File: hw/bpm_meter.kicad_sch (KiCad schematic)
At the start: 57 parts, among them J1 weidmueller_SL5.08HC-06-90, J2 weidmueller_SL5.08HC-10-90, Q1 AO3400A, SW1 dip_switch_SPST16, U1 SP3485EN-L/TR, U2 AOZ1282CI

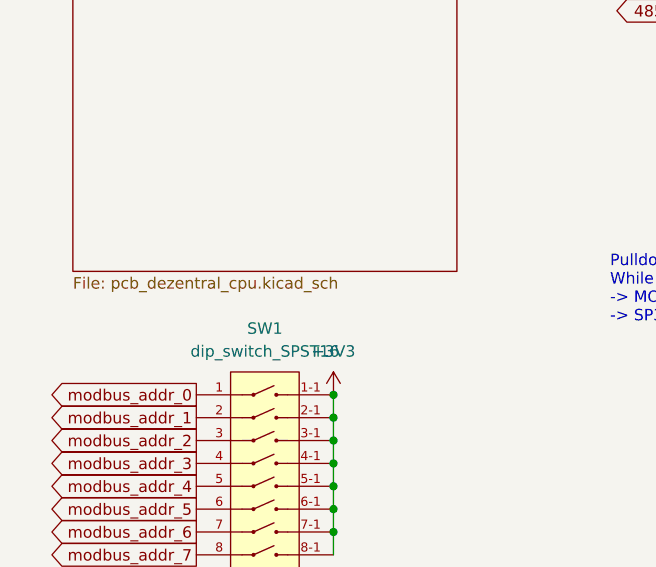
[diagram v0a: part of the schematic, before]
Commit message: Renamed the KiCad project
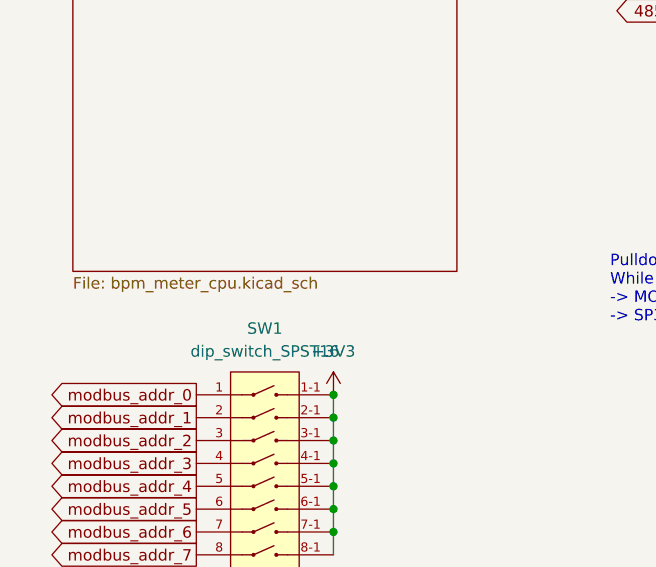
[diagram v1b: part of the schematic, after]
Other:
- sheet cpu: file pcb_dezentral_cpu.kicad_sch -> bpm_meter_cpu.kicad_sch
- company: www.positron.ch -> (none)
- title: Heizung Pünterswis - pcb_dezentral -> Schen-Key BPM Meter

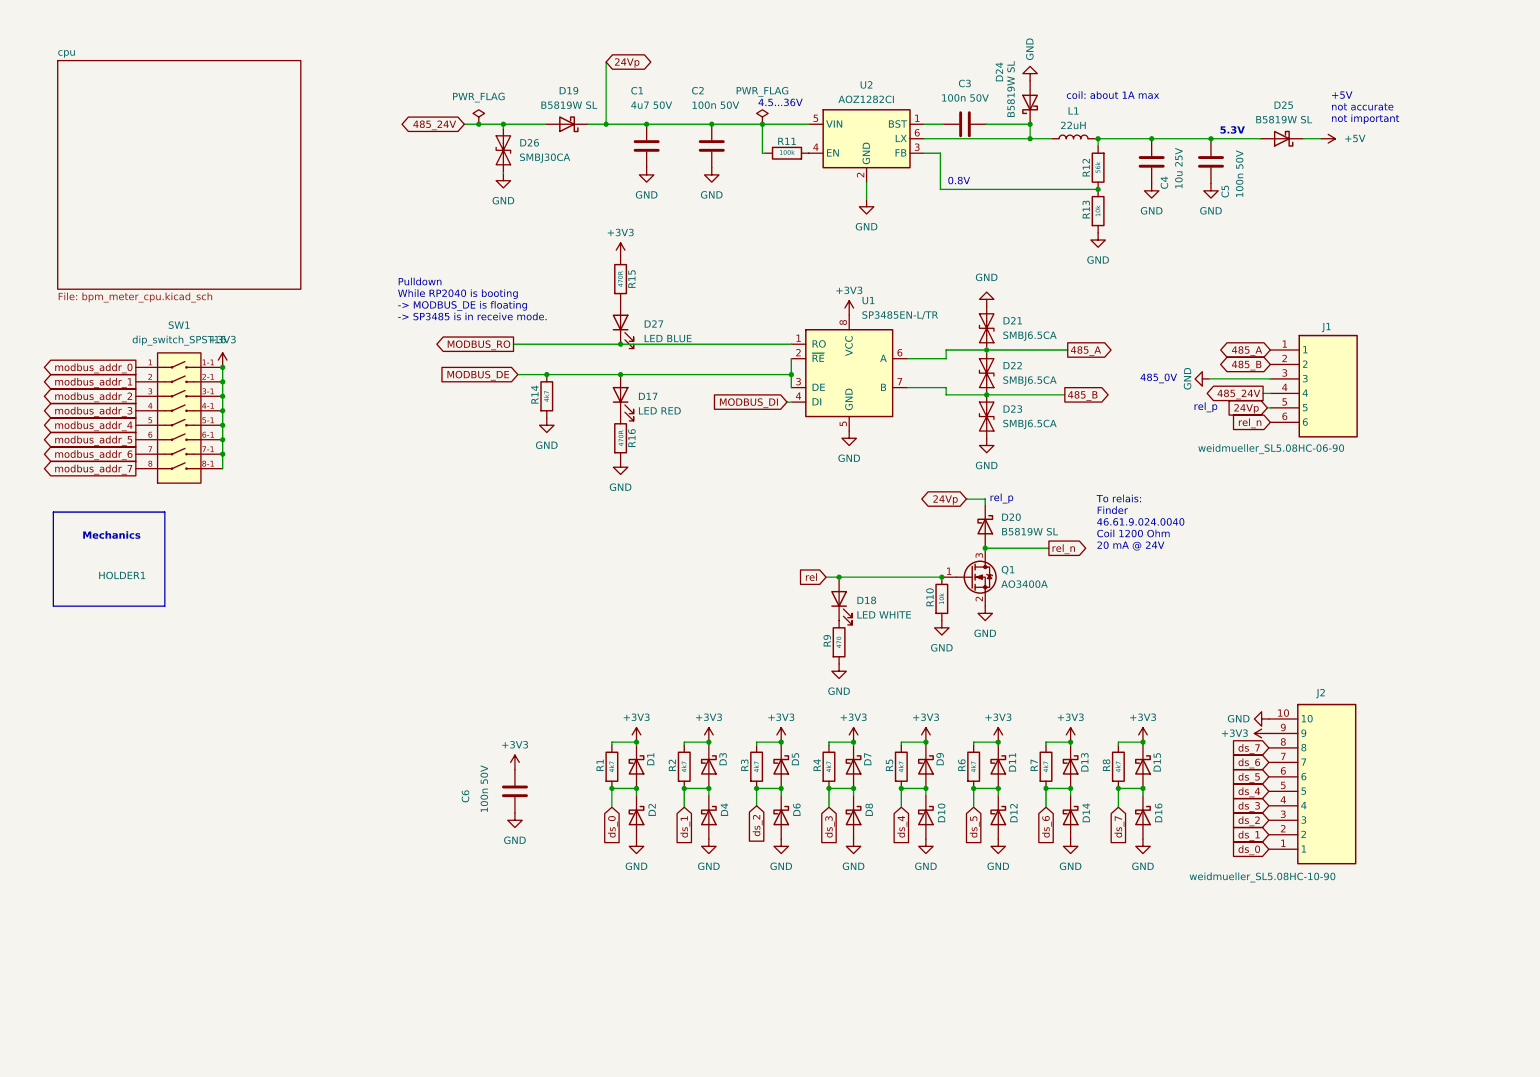
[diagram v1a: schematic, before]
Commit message: Removed unused stuff and added beat input
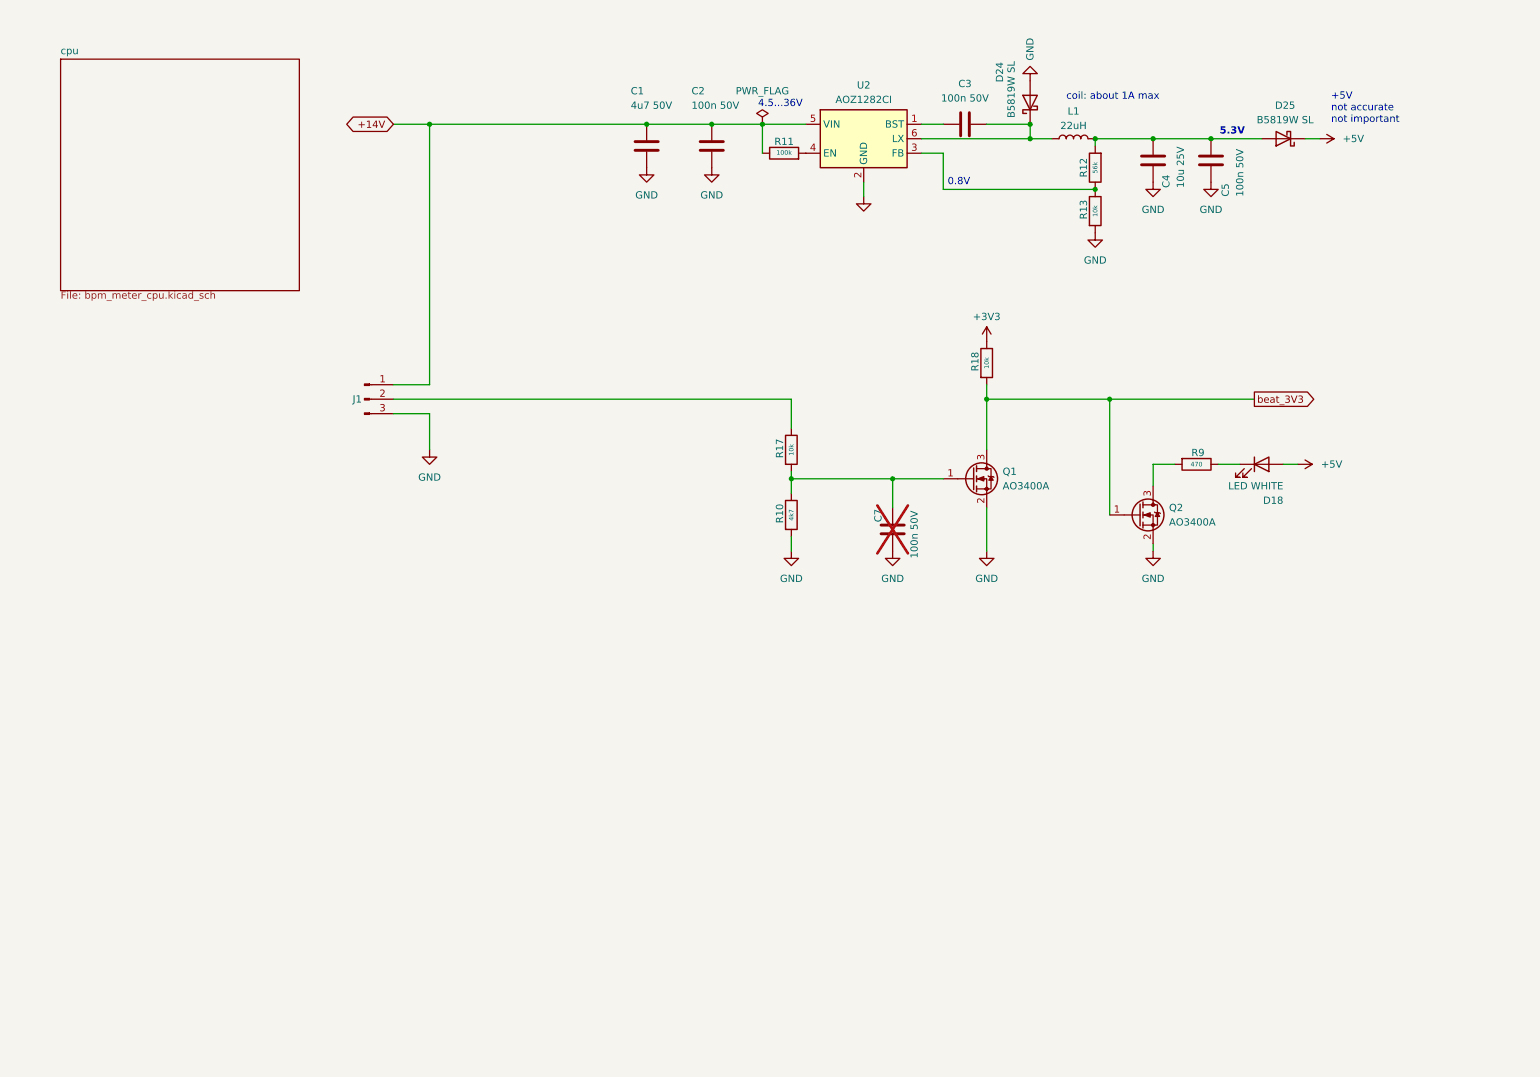
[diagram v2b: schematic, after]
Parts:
- removed C6: 100n 50V, Diode_SMD:D_0805_2012Metric, symbol Device:C
- removed D1, D10, D11, D12, D13, D14, D15, D16, D19, D2, D20, D3, D4, D5, D6, D7, D8, D9: B5819W SL, Diode_SMD:D_SOD-123, symbol Device:D_Schottky
- removed D17: LED RED, 00_project_library:LED_0603_1608Metric, symbol 00_project_library:LED RED
- removed D21, D22, D23: SMBJ6.5CA, Diode_SMD:D_SMB, symbol Diode:SMAJ64CA
- removed D26: SMBJ30CA, Diode_SMD:D_SMB, symbol Diode:SMAJ64CA
- removed D27: LED BLUE, 00_project_library:LED_0603_1608Metric, symbol 00_project_library:LED BLUE
- removed J1: weidmueller_SL5.08HC-06-90, 00_project_library:weidmueller_SL5.08HC-06-90, symbol 00_project_library:weidmueller_SL5.08HC-06-90
- removed J2: weidmueller_SL5.08HC-10-90, 00_project_library:weidmueller_SL5.08HC-10-90, symbol 00_project_library:weidmueller_SL5.08HC-10-90
- removed R1, R14, R2, R3, R4, R5, R6, R7, R8: 4k7, Resistor_SMD:R_0402_1005Metric_Pad0.72x0.64mm_HandSolder, symbol Device:R
- removed R15, R16: 470R, Resistor_SMD:R_0402_1005Metric_Pad0.72x0.64mm_HandSolder, symbol Device:R
- removed SW1: dip_switch_SPST16, 00_project_library:dip_switch_SPST16, symbol 00_project_library:dip_switch_SPST16
- removed U1: SP3485EN-L/TR, Package_SO:SOIC-8_3.9x4.9mm_P1.27mm, symbol 00_project_library:modbus_SP3485EN
- added C7: 100n 50V, Diode_SMD:D_0805_2012Metric, symbol Device:C
- added J1: Conn_01x03_Pin, Connector_PinHeader_2.54mm:PinHeader_1x03_P2.54mm_Vertical, symbol Connector:Conn_01x03_Pin
- added Q2: AO3400A, Package_TO_SOT_SMD:SOT-23, symbol Transistor_FET:AO3400A
- added R17, R18: 10k, Resistor_SMD:R_0402_1005Metric_Pad0.72x0.64mm_HandSolder, symbol Device:R
- R10: value 10k -> 4k7
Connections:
- net +3V3: now also R18.1
- net +5V: now also D18.2 (A)
- net GND: now also C7.2, J1.3 (Pin_3), Q2.2 (S); no longer R9.2
- net 24Vp renamed +14V
- net +14V: now also J1.1 (Pin_1)
- net rel: no longer names the net of Q1.1 (G), R10.1
- net rel: now also C7.1, R17.2; no longer D18.2 (A)
- net rel_n renamed beat_3V3
- net beat_3V3: now also Q2.1 (G), R18.2
- new net: Q2.3 (D), R9.2
- new net: J1.2 (Pin_2), R17.1
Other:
- note removed: "485_0V"
- note removed: "Mechanics"
- note removed: "Pulldown While RP2040 is booting -> MODBUS_DE is floating -> SP3485 is in receive mode."
- note removed: "To relais: Finder 46.61.9.024.0040 Coil 1200 Ohm 20 mA @ 24V"
- note removed: "rel_p"
- moved on the sheet: D18, Q1, R11, R12, R13, R9, U2

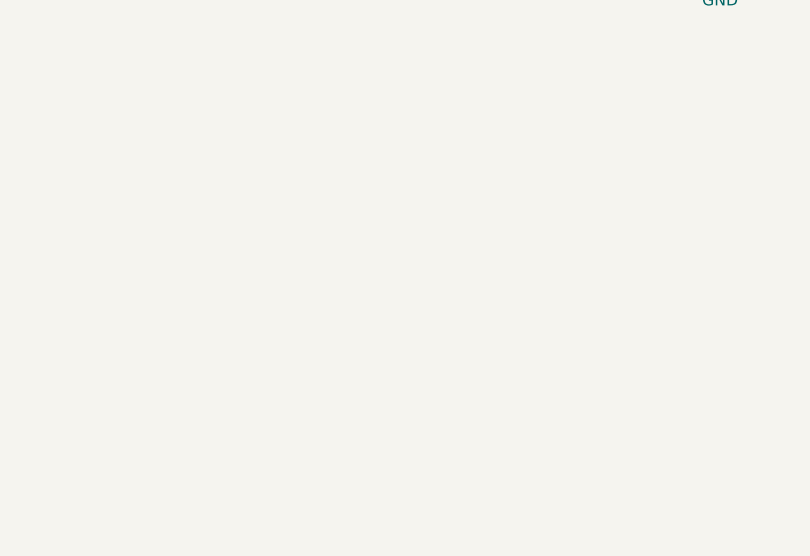
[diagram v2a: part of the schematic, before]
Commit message: Added a 7-segment LED symbol
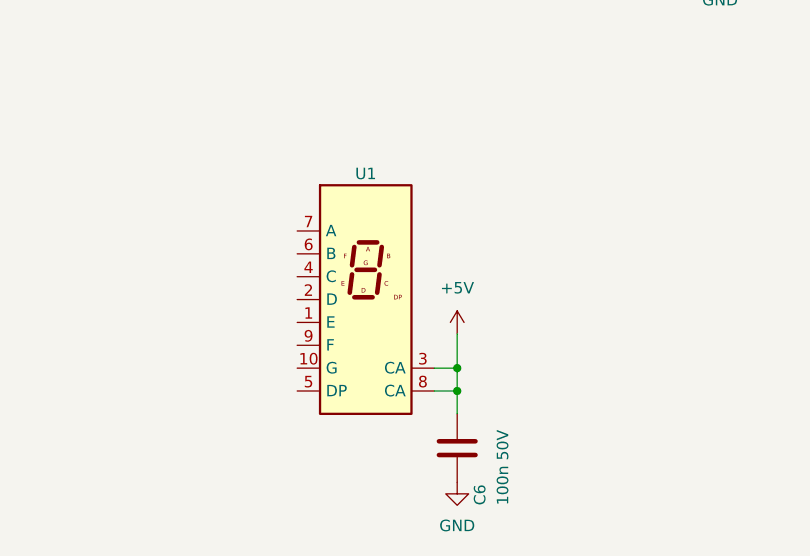
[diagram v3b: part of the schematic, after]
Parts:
- added C6: 100n 50V, Diode_SMD:D_0805_2012Metric, symbol Device:C
- added U1: SLS0391FR1A1GD, Display_7Segment:KCSC02-105, symbol Display_Character:KCSA02-105
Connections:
- net +5V: now also C6.2, U1.3 (CA), U1.8 (CA)
- net GND: now also C6.1
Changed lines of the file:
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@@
   (junction (at 194.31 31.75) (diameter 0) (color 0 0 0 0)
   )
+  (junction (at 123.19 154.94) (diameter 0) (color 0 0 0 0)
+  )
   (junction (at 215.9 34.29) (diameter 0) (color 0 0 0 0)
   )
@@
   (junction (at 170.18 93.98) (diameter 0) (color 0 0 0 0)
   )
+  (junction (at 123.19 152.4) (diameter 0) (color 0 0 0 0)
+  )
   (wire (pts (xy 186.69 80.01) (xy 186.69 88.9))
     (stroke (width 0) (type default))
@@
     (stroke (width 0) (type default))
   )
+  (wire (pts (xy 120.65 154.94) (xy 123.19 154.94))
+    (stroke (width 0) (type default))
+  )
   (wire (pts (xy 194.31 34.29) (xy 198.12 34.29))
     (stroke (width 0) (type default))
@@
     (stroke (width 0) (type default))
   )
+  (wire (pts (xy 123.19 157.48) (xy 123.19 154.94))
+    (stroke (width 0) (type default))
+  )
   (wire (pts (xy 175.26 31.75) (xy 179.07 31.75))
     (stroke (width 0) (type default))
   )
+  (wire (pts (xy 120.65 152.4) (xy 123.19 152.4))
+    (stroke (width 0) (type default))
+  )
+  (wire (pts (xy 123.19 148.59) (xy 123.19 152.4))
+    (stroke (width 0) (type default))
+  )
   (wire (pts (xy 205.74 35.56) (xy 205.74 34.29))
     (stroke (width 0) (type default))
@@
   )
   (wire (pts (xy 194.31 31.75) (xy 194.31 34.29))
+    (stroke (width 0) (type default))
+  )
+  (wire (pts (xy 123.19 152.4) (xy 123.19 154.94))
     (stroke (width 0) (type default))
   )
@@
     )
   )
+  (symbol (lib_id "power:+5V") (at 123.19 148.59 0) (unit 1)
+    (in_bom yes) (on_board yes) (dnp no) (fields_autoplaced)
+    (property "Reference" "#PWR05" (at 123.19 152.4 0)
+      (effects (font (size 1.27 1.27)) hide)
+    )
+    (property "Value" "+5V" (at 123.19 143.51 0)
+      (effects (font (size 1.27 1.27)))
+    )
+    (property "Footprint" "" (at 123.19 148.59 0)
+      (effects (font (size 1.27 1.27)) hide)
+    )
+    (property "Datasheet" "" (at 123.19 148.59 0)
+      (effects (font (size 1.27 1.27)) hide)
+    )
+    (pin "1")
+    (instances
+      (project "bpm_meter"
+        (path "/35c47459-45a7-4753-acae-c8b47e7575e1"
+          (reference "#PWR05") (unit 1)
+        )
+      )
+    )
+  )
   (symbol (lib_id "power:GND") (at 215.9 106.68 0) (unit 1)
     (in_bom yes) (on_board yes) (dnp no)
@@
     )
   )
+  (symbol (lib_id "power:GND") (at 123.19 165.1 0) (unit 1)
+    (in_bom yes) (on_board yes) (dnp no) (fields_autoplaced)
+    (property "Reference" "#PWR06" (at 123.19 171.45 0)
+      (effects (font (size 1.27 1.27)) hide)
+    )
+    (property "Value" "GND" (at 123.19 169.926 0)
+      (effects (font (size 1.27 1.27)))
+    )
+    (property "Footprint" "" (at 123.19 165.1 0)
+      (effects (font (size 1.27 1.27)) hide)
+    )
+    (property "Datasheet" "" (at 123.19 165.1 0)
+      (effects (font (size 1.27 1.27)) hide)
+    )
+    (pin "1")
+    (instances
+      (project "bpm_meter"
+        (path "/35c47459-45a7-4753-acae-c8b47e7575e1"
+          (reference "#PWR06") (unit 1)
+        )
+      )
+    )
+  )
   (symbol (lib_id "power:GND") (at 138.43 39.37 0) (unit 1)
     (in_bom yes) (on_board yes) (dnp no) (fields_autoplaced)
@@
         (path "/35c47459-45a7-4753-acae-c8b47e7575e1"
           (reference "#PWR027") (unit 1)
+        )
+      )
+    )
+  )
+  (symbol (lib_id "Device:C") (at 123.19 161.29 180) (unit 1)
+    (in_bom yes) (on_board yes) (dnp no)
+    (property "Reference" "C6" (at 125.73 167.64 90)
+      (effects (font (size 1.27 1.27)) (justify right))
+    )
+    (property "Value" "100n 50V" (at 128.27 167.64 90)
+      (effects (font (size 1.27 1.27)) (justify right))
+    )
+    (property "Footprint" "Diode_SMD:D_0805_2012Metric" (at 122.2248 157.48 0)
+      (effects (font (size 1.27 1.27)) hide)
+    )
+    (property "Datasheet" "~" (at 123.19 161.29 0)
+      (effects (font (size 1.27 1.27)) hide)
+    )
+    (property "JLC" "C49678" (at 123.19 161.29 0)
+      (effects (font (size 1.27 1.27)) hide)
+    )
+    (pin "1")
+    (pin "2")
+    (instances
+      (project "bpm_meter"
+        (path "/35c47459-45a7-4753-acae-c8b47e7575e1"
+          (reference "C6") (unit 1)
         )
       )
@@
         )
       )
+    )
+  )
+  (symbol (lib_id "Display_Character:KCSA02-105") (at 113.03 144.78 0) (unit 1)
+    (in_bom yes) (on_board yes) (dnp no)
+    (property "Reference" "U1" (at 113.03 130.81 0)
+      (effects (font (size 1.27 1.27)))
+    )
+    (property "Value" "SLS0391FR1A1GD" (at 113.03 129.54 0)
+      (effects (font (size 1.27 1.27)) hide)
+    )
+    (property "Footprint" "Display_7Segment:KCSC02-105" (at 113.03 160.02 0)
+      (effects (font (size 1.27 1.27)) hide)
+    )
+    (property "Datasheet" "" (at 100.33 132.715 0)
+      (effects (font (size 1.27 1.27)) (justify left) hide)
+    )
+    (property "JLC" "C2913076" (at 113.03 144.78 0)
+      (effects (font (size 1.27 1.27)) hide)
+    )
+    (pin "6")
+    (pin "2")
+    (pin "7")
+    (pin "3")
+    (pin "8")
+    (pin "9")
+    (pin "10")
+    (pin "1")
+    (pin "5")
+    (pin "4")
+    (instances
+      (project "bpm_meter"
+        (path "/35c47459-45a7-4753-acae-c8b47e7575e1"
+          (reference "U1") (unit 1)
+        )
+      )
